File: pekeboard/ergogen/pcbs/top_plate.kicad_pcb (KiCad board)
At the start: 2 copper layers, 161.8 x 135.1 mm, 0 parts

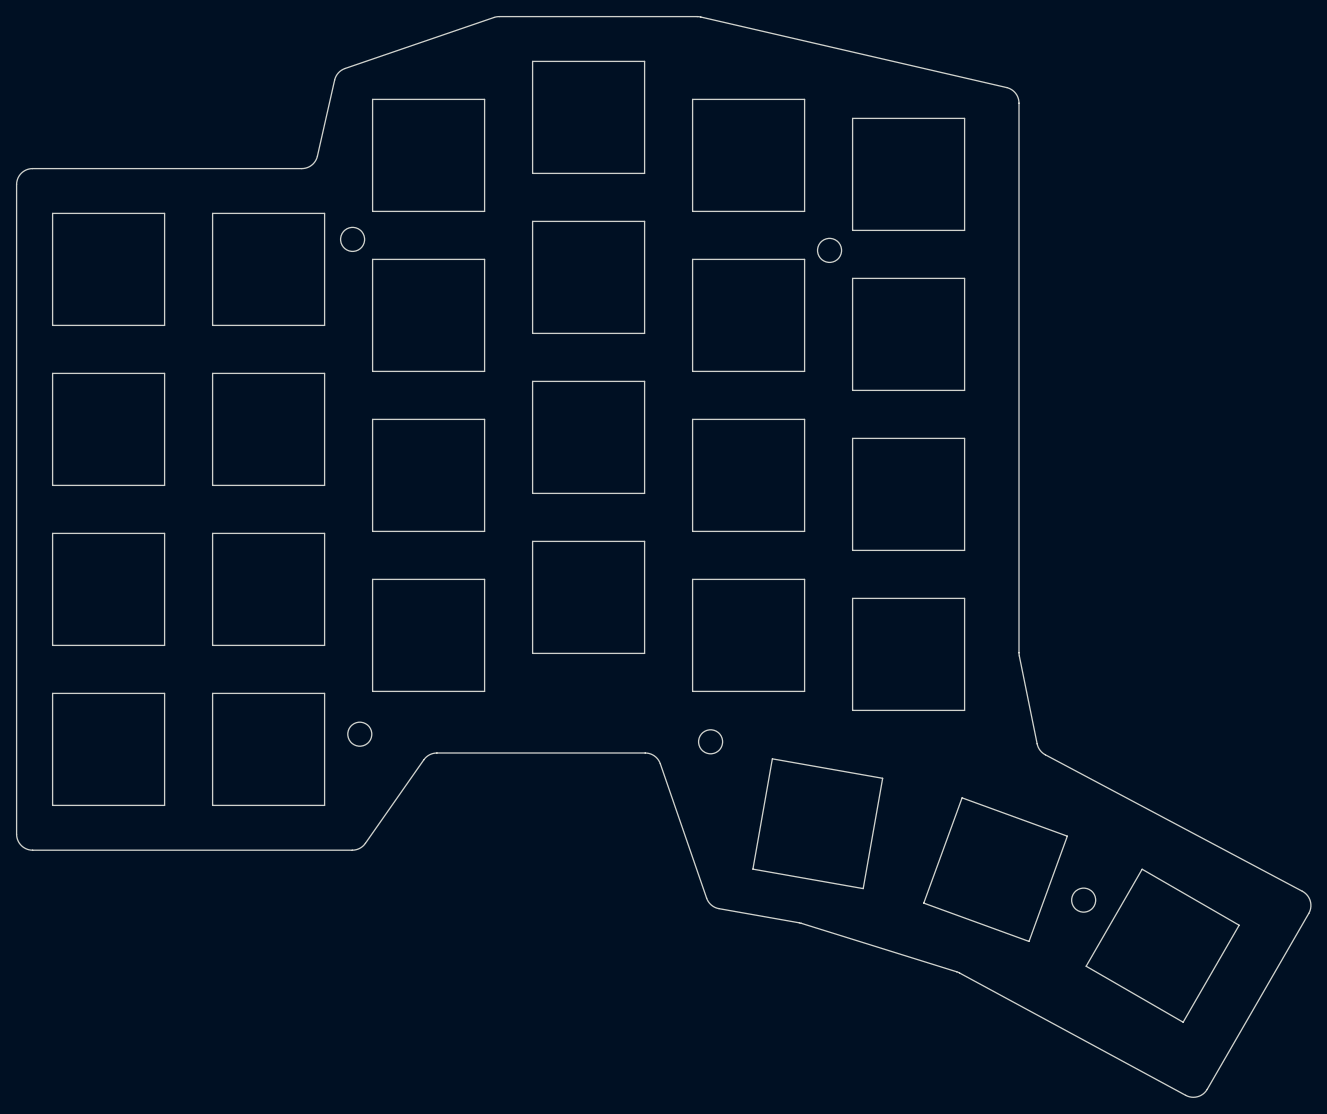
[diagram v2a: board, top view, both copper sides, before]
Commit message: Fixing keys spacing More case and battery space refinements
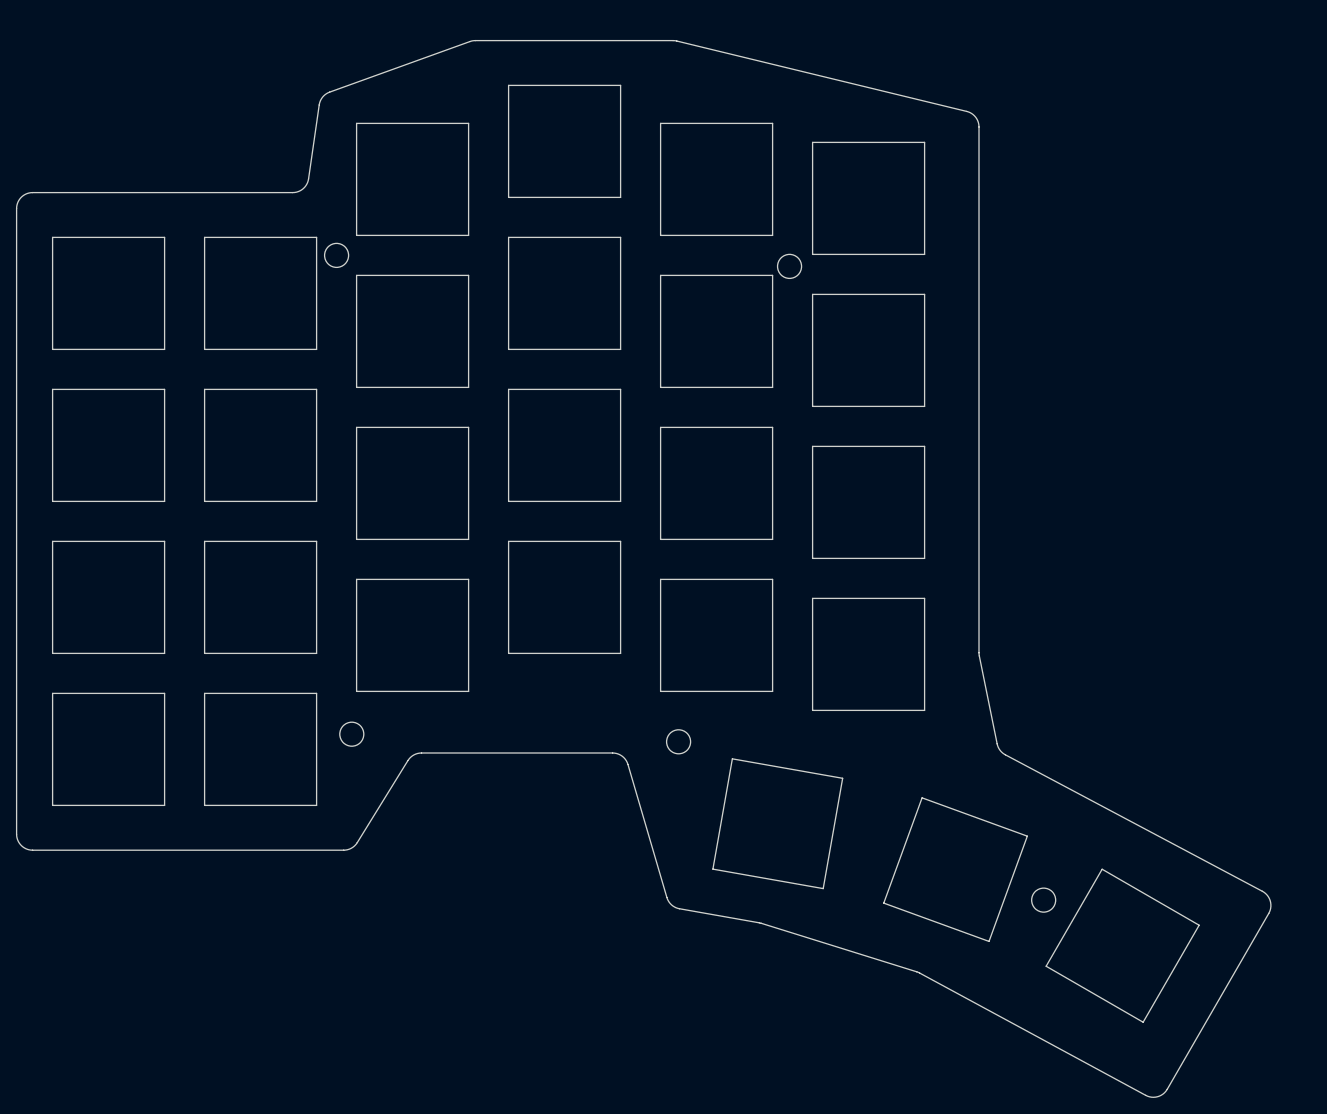
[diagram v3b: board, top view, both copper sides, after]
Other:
- board size 161.8 x 135.1 mm -> 156.8 x 132.1 mm

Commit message: Extreme trimming
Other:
- board size 156.8 x 132.1 mm -> 150.9 x 124.7 mm

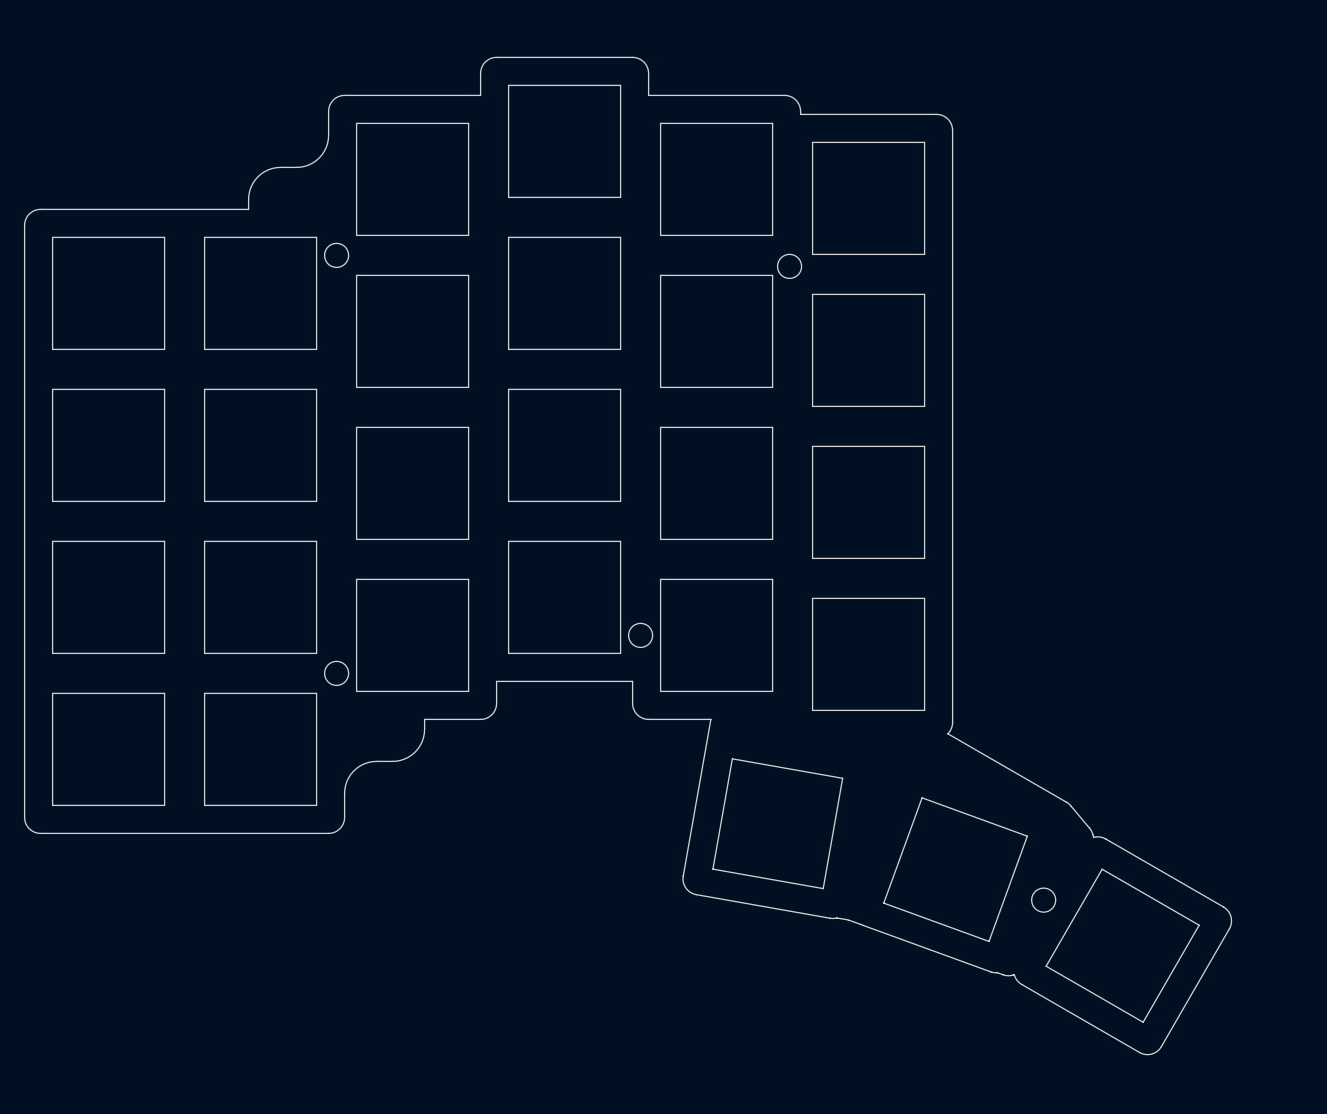
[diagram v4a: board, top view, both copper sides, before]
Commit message: Adjusting mounting holes
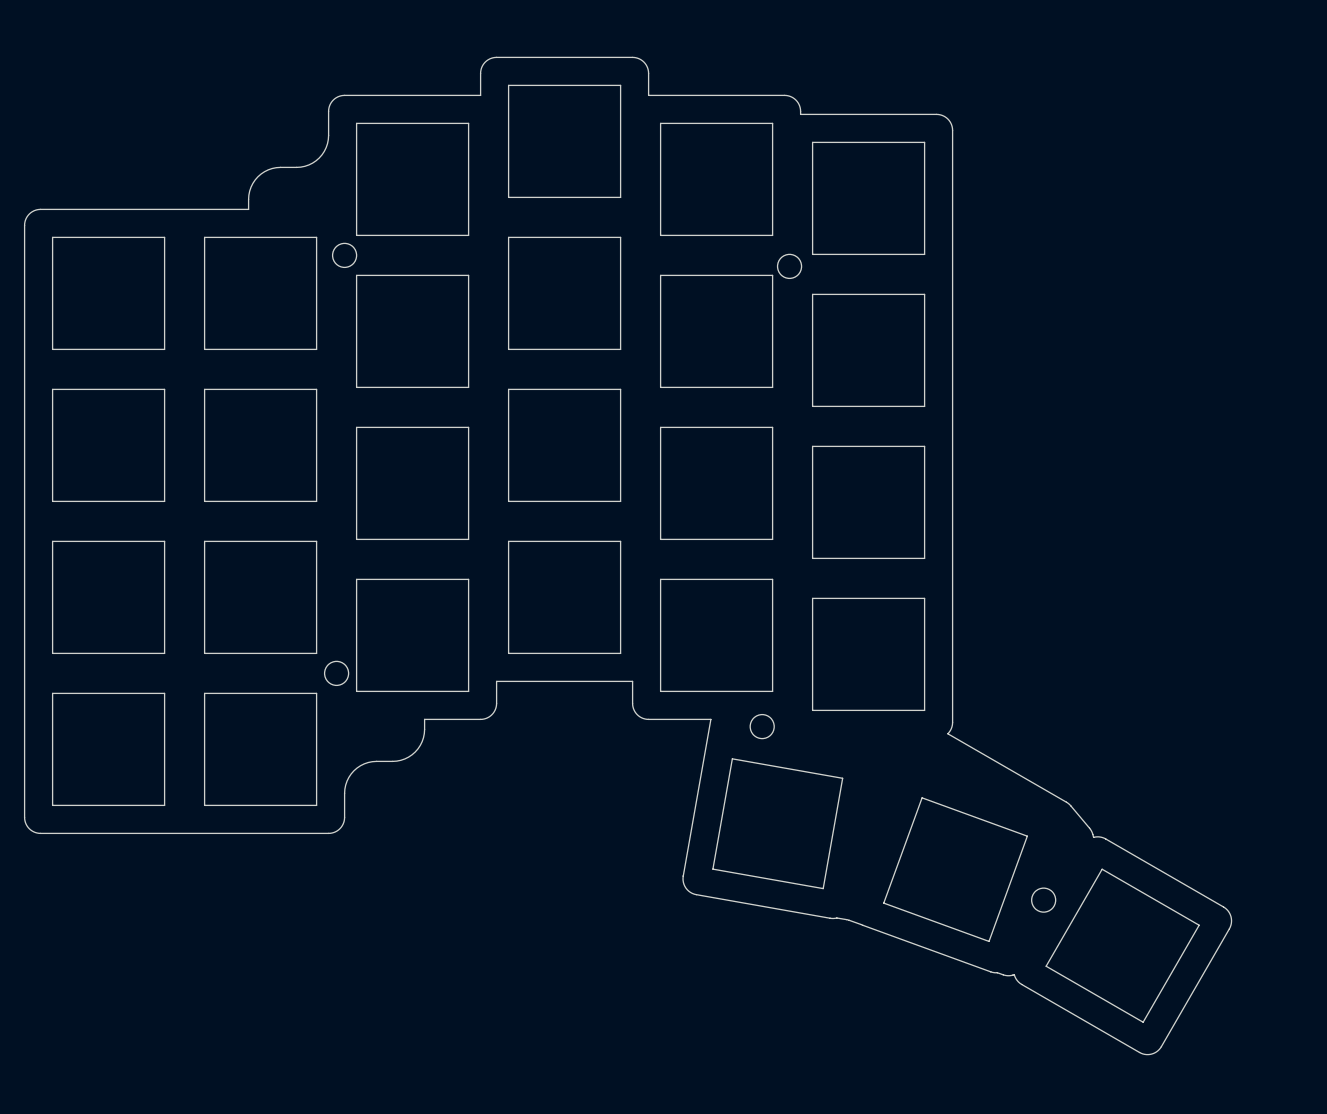
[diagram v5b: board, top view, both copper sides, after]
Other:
- outline, holes or cut-outs redrawn

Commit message: Fix mounting hole outside PCB
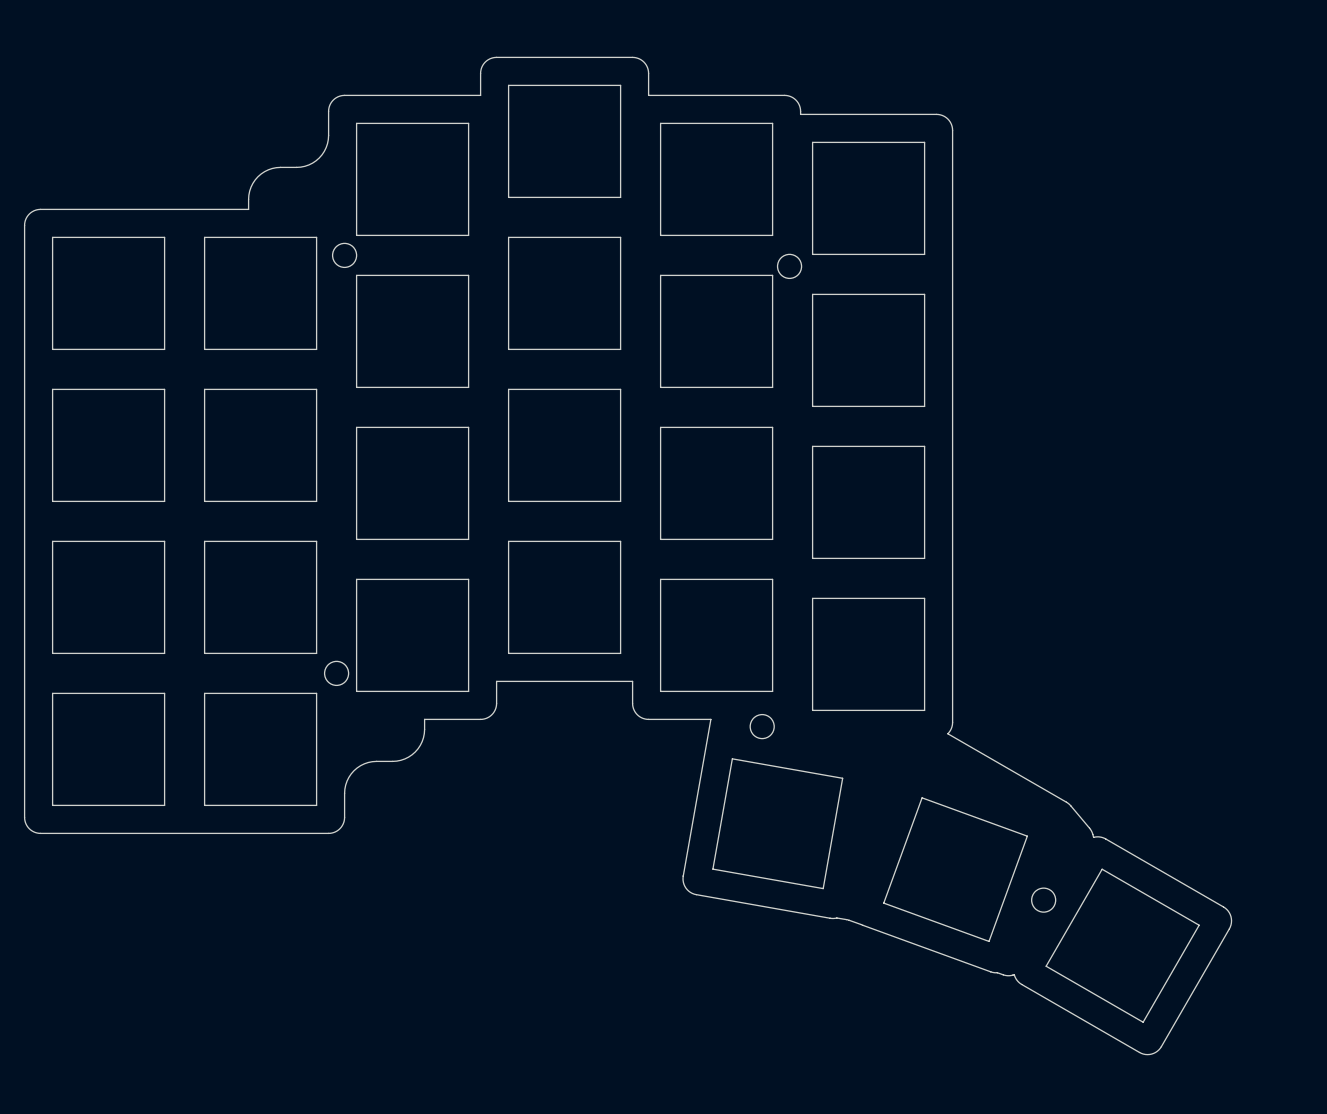
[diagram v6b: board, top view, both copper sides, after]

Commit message: reversible diodes removing fill zone
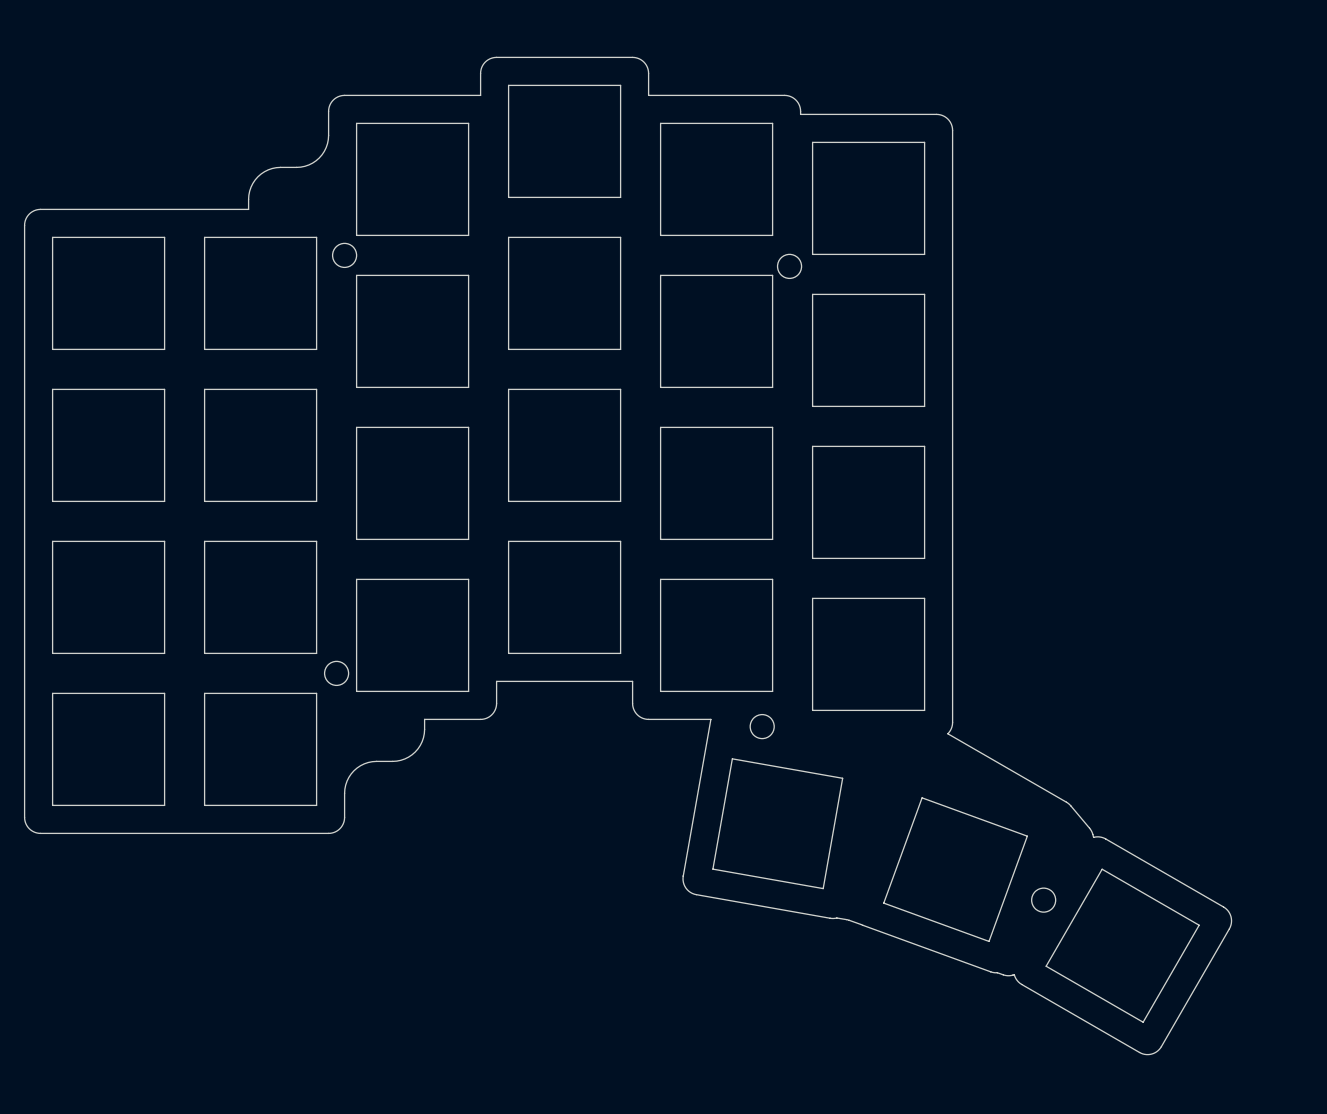
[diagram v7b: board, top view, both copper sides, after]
